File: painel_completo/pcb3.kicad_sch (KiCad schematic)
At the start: 13 parts, among them J11 Conn_02x10_Odd_Even, J19 Conn_02x10_Odd_Even

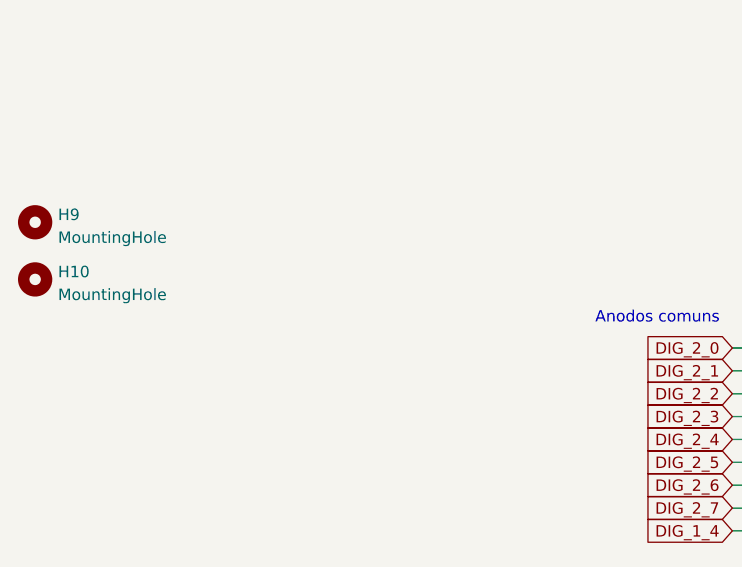
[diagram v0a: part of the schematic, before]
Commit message: adição furos fixação e alteração máscara de componentes
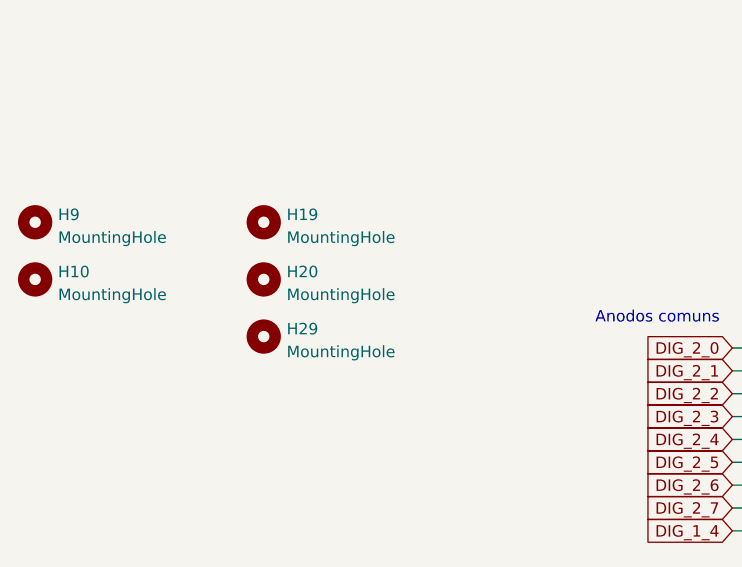
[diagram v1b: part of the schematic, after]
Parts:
- added H19, H20, H29: MountingHole, MountingHole:MountingHole_3.2mm_M3, symbol Mechanical:MountingHole
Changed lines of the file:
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@@
     (pin "2")
+  )
+  (symbol (lib_id "Mechanical:MountingHole") (at 114.3 165.1 0) (unit 1)
+    (in_bom yes) (on_board yes) (fields_autoplaced)
+    (property "Reference" "H20" (id 0) (at 116.84 164.2653 0)
+      (effects (font (size 1.27 1.27)) (justify left))
+    )
+    (property "Value" "MountingHole" (id 1) (at 116.84 166.8022 0)
+      (effects (font (size 1.27 1.27)) (justify left))
+    )
+    (property "Footprint" "MountingHole:MountingHole_3.2mm_M3" (id 2) (at 114.3 165.1 0)
+      (effects (font (size 1.27 1.27)) hide)
+    )
+    (property "Datasheet" "~" (id 3) (at 114.3 165.1 0)
+      (effects (font (size 1.27 1.27)) hide)
+    )
   )
   (symbol (lib_id "Device:LED_Small") (at 288.29 102.87 90) (unit 1)
@@
     (pin "1")
     (pin "2")
+  )
+  (symbol (lib_id "Mechanical:MountingHole") (at 114.3 171.45 0) (unit 1)
+    (in_bom yes) (on_board yes) (fields_autoplaced)
+    (property "Reference" "H29" (id 0) (at 116.84 170.6153 0)
+      (effects (font (size 1.27 1.27)) (justify left))
+    )
+    (property "Value" "MountingHole" (id 1) (at 116.84 173.1522 0)
+      (effects (font (size 1.27 1.27)) (justify left))
+    )
+    (property "Footprint" "MountingHole:MountingHole_3.2mm_M3" (id 2) (at 114.3 171.45 0)
+      (effects (font (size 1.27 1.27)) hide)
+    )
+    (property "Datasheet" "~" (id 3) (at 114.3 171.45 0)
+      (effects (font (size 1.27 1.27)) hide)
+    )
   )
   (symbol (lib_id "Device:LED_Small") (at 248.92 102.87 90) (unit 1)
@@
     (pin "9")
   )
+  (symbol (lib_id "Mechanical:MountingHole") (at 114.3 158.75 0) (unit 1)
+    (in_bom yes) (on_board yes) (fields_autoplaced)
+    (property "Reference" "H19" (id 0) (at 116.84 157.9153 0)
+      (effects (font (size 1.27 1.27)) (justify left))
+    )
+    (property "Value" "MountingHole" (id 1) (at 116.84 160.4522 0)
+      (effects (font (size 1.27 1.27)) (justify left))
+    )
+    (property "Footprint" "MountingHole:MountingHole_3.2mm_M3" (id 2) (at 114.3 158.75 0)
+      (effects (font (size 1.27 1.27)) hide)
+    )
+    (property "Datasheet" "~" (id 3) (at 114.3 158.75 0)
+      (effects (font (size 1.27 1.27)) hide)
+    )
+  )
   (symbol (lib_id "Mechanical:MountingHole") (at 88.9 165.1 0) (unit 1)
